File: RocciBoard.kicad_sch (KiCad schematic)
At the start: 205 parts, among them J1 Battery, J10 M3, J11 I2C6, J12 Power, J13 M2, J14 I2C7, J2 I2C0, J3 I2C1, J4 I2C2, J5 I2C3, J6 M0, J7 I2C4, J8 M1, J9 I2C5, Q1 IRF 7424, Q2 2N7002, SW1 SW_DIP_x01, U1 LMR33630, U10 LM317_TO-252, U11 CJ431, U12 CJ431, U2 LM317_TO-252, U3 LM317_TO-252, U4 TPS3700, U5 TCA9548A, U6 DRV8871, U7 DRV8871, U8 DRV8871, U9 DRV8871

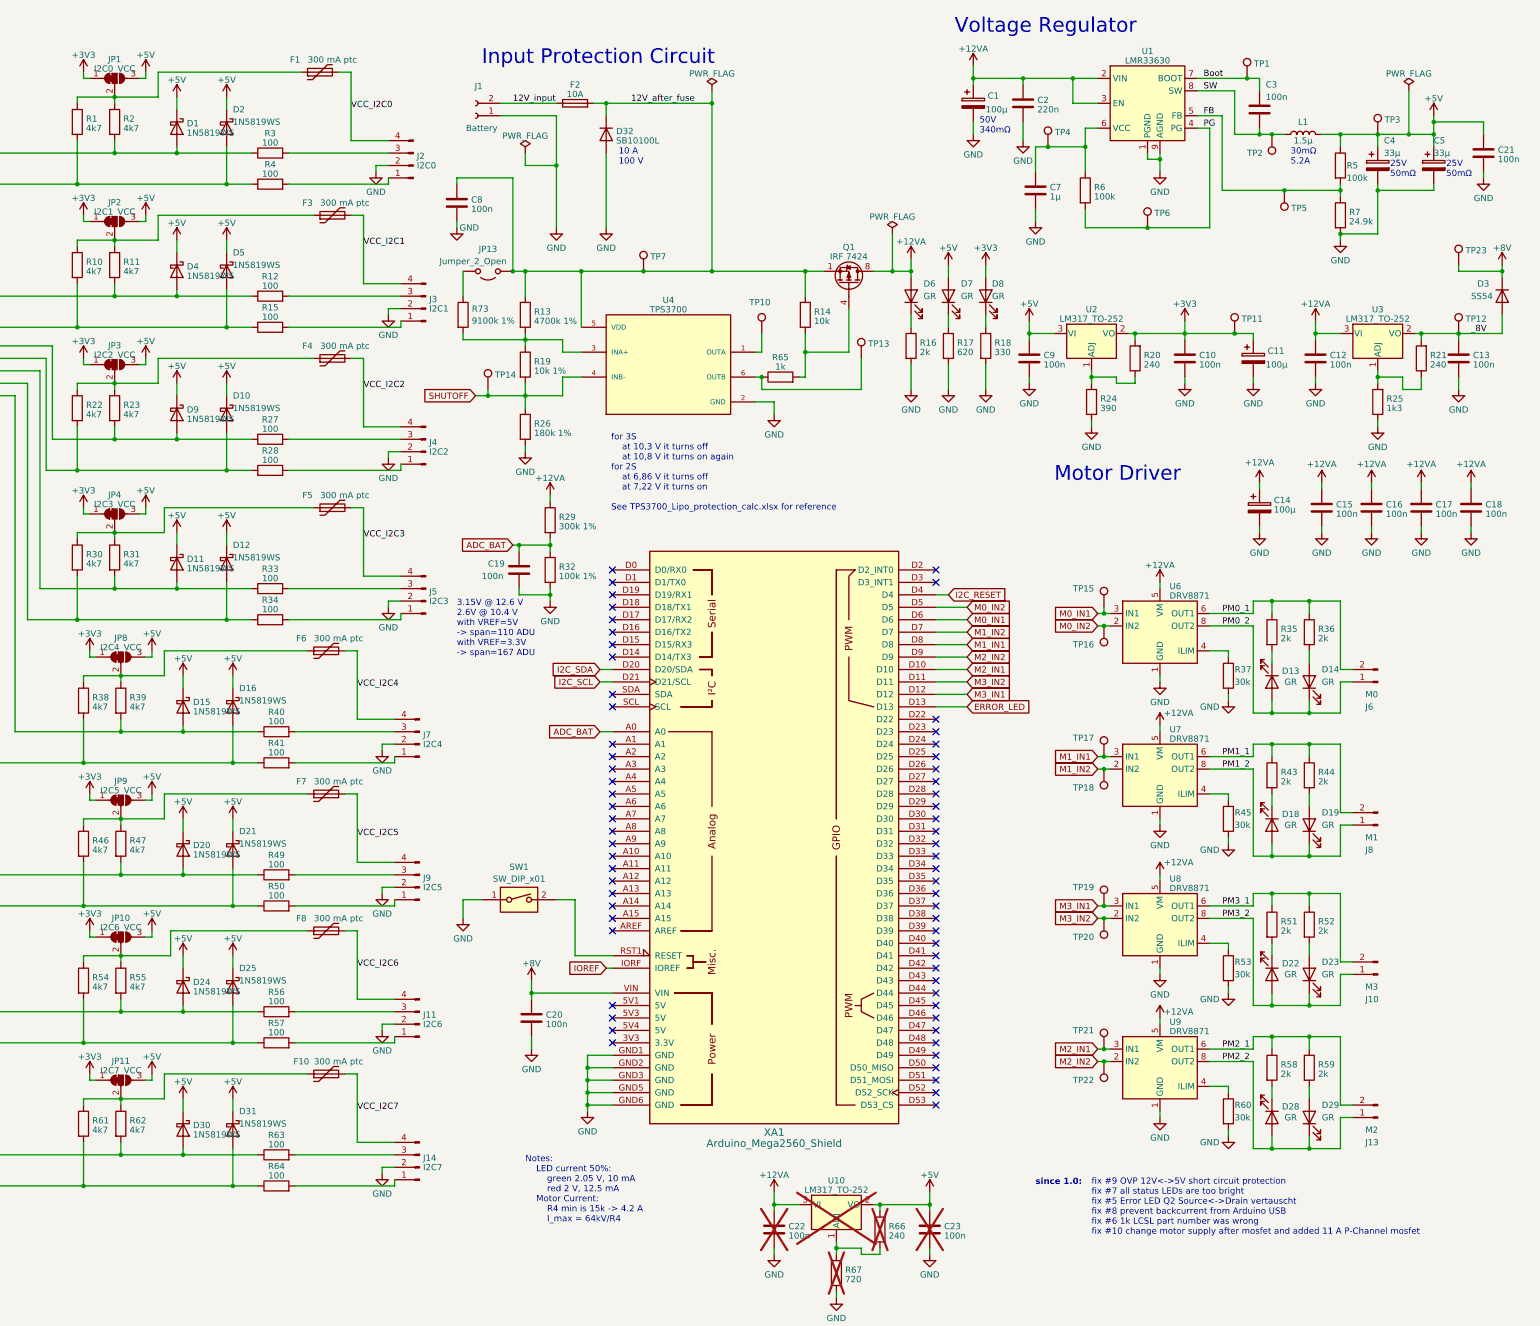
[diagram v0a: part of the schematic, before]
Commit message: add xt60 and spereate i2c pwr and data jumper
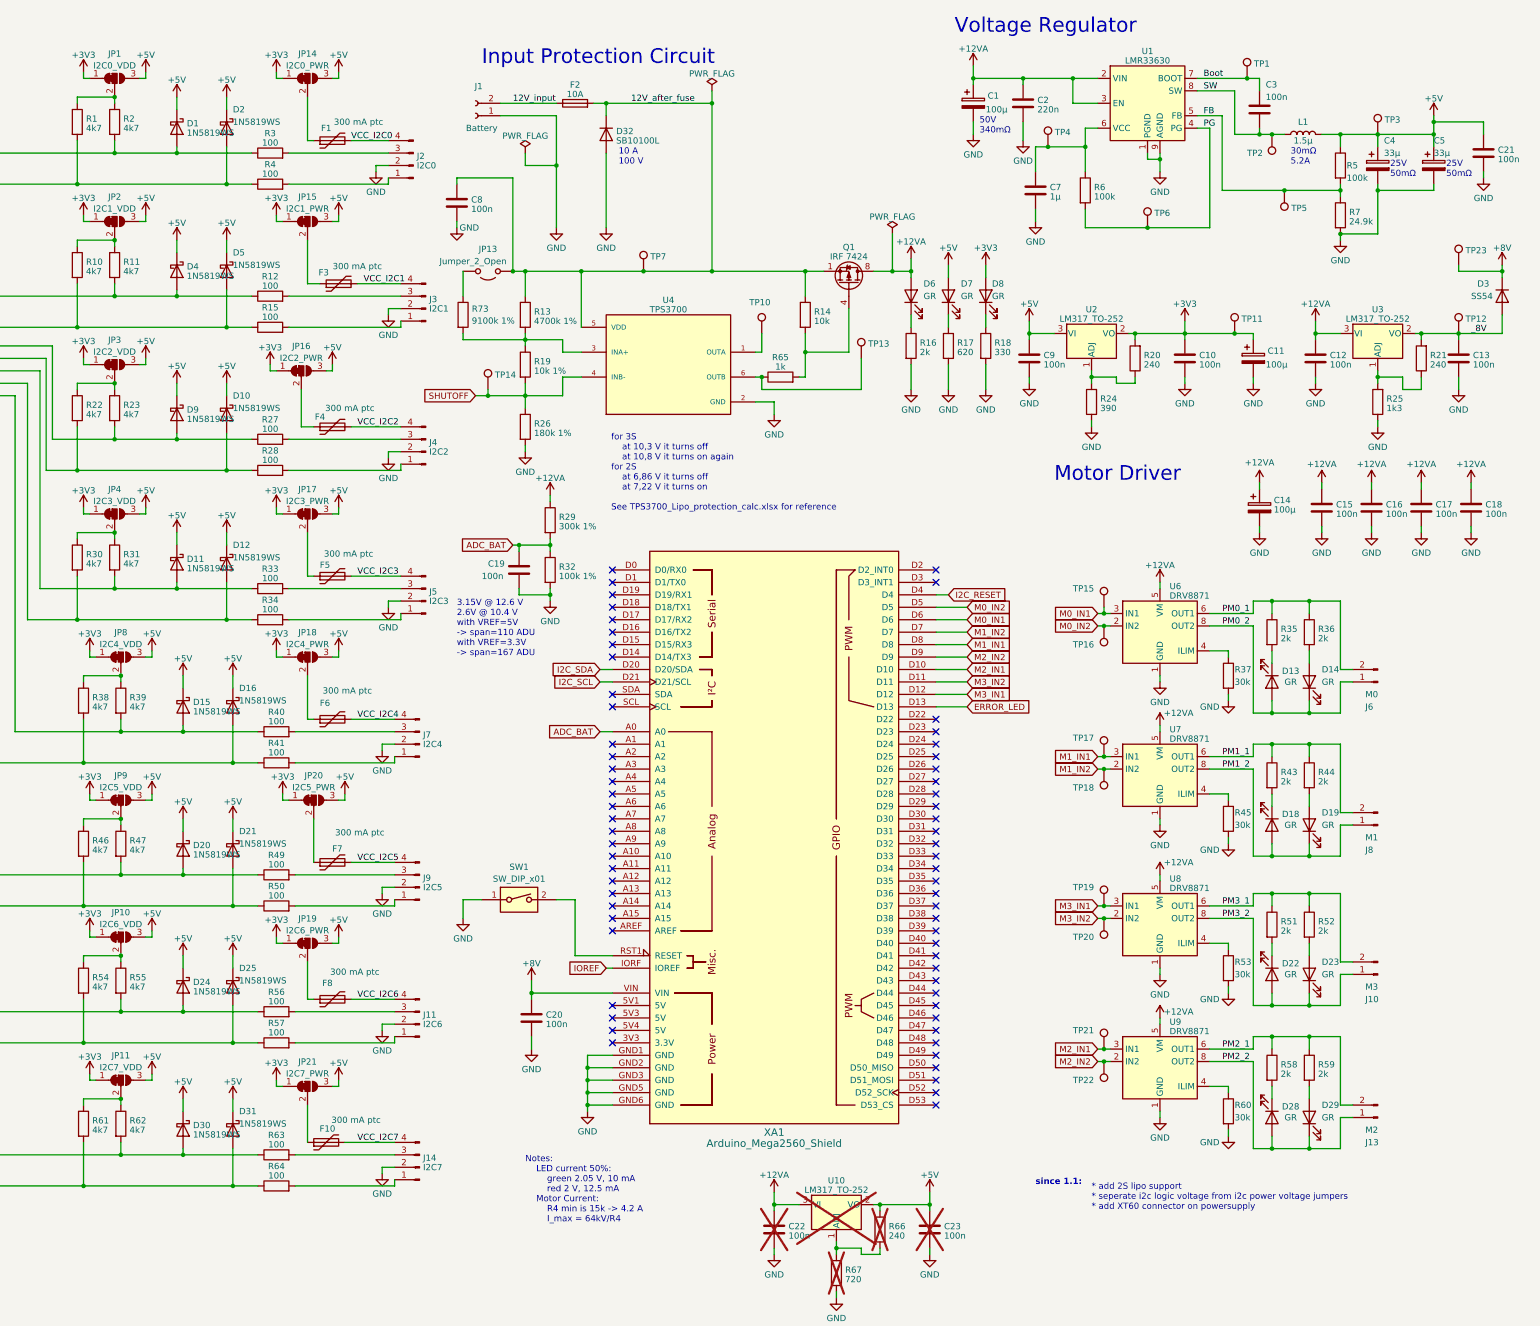
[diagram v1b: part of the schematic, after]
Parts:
- added JP14: I2C0_PWR, Jumper:SolderJumper-3_P1.3mm_Open_Pad1.0x1.5mm, symbol Jumper:SolderJumper_3_Bridged12
- added JP15: I2C1_PWR, Jumper:SolderJumper-3_P1.3mm_Open_Pad1.0x1.5mm, symbol Jumper:SolderJumper_3_Bridged12
- added JP16: I2C2_PWR, Jumper:SolderJumper-3_P1.3mm_Open_Pad1.0x1.5mm, symbol Jumper:SolderJumper_3_Bridged12
- added JP17: I2C3_PWR, Jumper:SolderJumper-3_P1.3mm_Open_Pad1.0x1.5mm, symbol Jumper:SolderJumper_3_Bridged12
- added JP18: I2C4_PWR, Jumper:SolderJumper-3_P1.3mm_Open_Pad1.0x1.5mm, symbol Jumper:SolderJumper_3_Bridged12
- added JP19: I2C6_PWR, Jumper:SolderJumper-3_P1.3mm_Open_Pad1.0x1.5mm, symbol Jumper:SolderJumper_3_Bridged12
- added JP20: I2C5_PWR, Jumper:SolderJumper-3_P1.3mm_Open_Pad1.0x1.5mm, symbol Jumper:SolderJumper_3_Bridged12
- added JP21: I2C7_PWR, Jumper:SolderJumper-3_P1.3mm_Open_Pad1.0x1.5mm, symbol Jumper:SolderJumper_3_Bridged12
- J1: footprint Connector_Phoenix_MSTB:PhoenixContact_MSTBVA_2,5_2-G_1x02_P5.00mm_Vertical -> Connector_AMASS:AMASS_XT60-M_1x02_P7.20mm_Vertical
- JP1: value I2C0_VCC -> I2C0_VDD
- JP10: value I2C6_VCC -> I2C6_VDD
- JP11: value I2C7_VCC -> I2C7_VDD
- JP13: footprint (none) -> Jumper:SolderJumper-2_P1.3mm_Open_Pad1.0x1.5mm
- JP2: value I2C1_VCC -> I2C1_VDD
- JP3: value I2C2_VCC -> I2C2_VDD
- JP4: value I2C3_VCC -> I2C3_VDD
- JP8: value I2C4_VCC -> I2C4_VDD
- JP9: value I2C5_VCC -> I2C5_VDD
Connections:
- net +3V3: now also JP14.1 (A), JP15.1 (A), JP16.1 (A), JP17.1 (A), JP18.1 (A), JP19.1 (A), JP20.1 (A), JP21.1 (A)
- net +5V: now also JP14.3 (B), JP15.3 (B), JP16.3 (B), JP17.3 (B), JP18.3 (B), JP19.3 (B), JP20.3 (B), JP21.3 (B)
- net at JP11.2 (C), R61.1, R62.1: no longer F10.1
- net at JP3.2 (C), R22.1, R23.1: no longer F4.1
- net at JP10.2 (C), R54.1, R55.1: no longer F8.1
- net at JP2.2 (C), R10.1, R11.1: no longer F3.1
- net at JP8.2 (C), R38.1, R39.1: no longer F6.1
- net at JP1.2 (C), R1.1, R2.1: no longer F1.1
- net at JP9.2 (C), R46.1, R47.1: no longer F7.1
- net at JP4.2 (C), R30.1, R31.1: no longer F5.1
- new net: F5.1, JP17.2 (C)
- new net: F1.1, JP14.2 (C)
- new net: F6.1, JP18.2 (C)
- new net: F10.1, JP21.2 (C)
- new net: F8.1, JP19.2 (C)
- new net: F4.1, JP16.2 (C)
- new net: F3.1, JP15.2 (C)
- new net: F7.1, JP20.2 (C)
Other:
- note added: "* add 2S lipo support * seperate i2c logic voltage from i2c power voltage jumpers * add XT60 connector on powersupply"
- note added: "since 1.1:"
- note removed: "fix #9 OVP 12V<->5V short circuit protection fix #7 all status LEDs are too bright fix #5 Error LED Q2 Source<->Drain vertauscht fix #8 prevent backcurrent from Arduino USB fix #6 1k LCSL part number was wrong fix #10 change motor supply after mosfet and added 11 A P-Channel mosfet"
- note removed: "since 1.0:"
- moved on the sheet: F1, F10, F3, F4, F5, F6, F7, F8

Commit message: more progress with nxt shield
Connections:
- net VCC_UF_I2C3: now reaches F5.1, JP17.2 (C)
- net VCC_UF_I2C0: now reaches F1.1, JP14.2 (C)
- net VCC_UF_I2C4: now reaches F6.1, JP18.2 (C)
- net VCC_UF_I2C7: now reaches F10.1, JP21.2 (C)
- net VCC_UF_I2C6: now reaches F8.1, JP19.2 (C)
- net VCC_UF_I2C2: now reaches F4.1, JP16.2 (C)
- net VCC_UF_I2C1: now reaches F3.1, JP15.2 (C)
- net VCC_UF_I2C5: now reaches F7.1, JP20.2 (C)
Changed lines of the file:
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@@
+		)
+	)
+	(label "VCC_UF_I2C1"
+		(at 158.75 65.0989 0)
+		(effects
+			(font
+				(size 1.27 1.27)
+			)
+			(justify left bottom)
 		)
 	)
@@
 		)
 	)
+	(label "VCC_UF_I2C4"
+		(at 158.75 152.4 0)
+		(effects
+			(font
+				(size 1.27 1.27)
+			)
+			(justify left bottom)
+		)
+	)
+	(label "VCC_UF_I2C0"
+		(at 158.75 35.56 0)
+		(effects
+			(font
+				(size 1.27 1.27)
+			)
+			(justify left bottom)
+		)
+	)
 	(label "VCC_I2C4"
 		(at 168.91 160.02 0)
@@
 		)
 	)
+	(label "VCC_UF_I2C6"
+		(at 158.75 209.55 0)
+		(effects
+			(font
+				(size 1.27 1.27)
+			)
+			(justify left bottom)
+		)
+	)
 	(label "PM3_2"
 		(at 345.44 200.66 0)
@@
 		)
 	)
+	(label "VCC_UF_I2C3"
+		(at 158.75 123.19 0)
+		(effects
+			(font
+				(size 1.27 1.27)
+			)
+			(justify left bottom)
+		)
+	)
 	(label "VCC_I2C1"
 		(at 170.18 71.12 0)
@@
 		)
 	)
+	(label "VCC_UF_I2C5"
+		(at 160.02 181.61 0)
+		(effects
+			(font
+				(size 1.27 1.27)
+			)
+			(justify left bottom)
+		)
+	)
 	(label "VCC_I2C5"
 		(at 168.91 189.23 0)
@@
 		)
 	)
+	(label "VCC_UF_I2C2"
+		(at 157.48 95.25 0)
+		(effects
+			(font
+				(size 1.27 1.27)
+			)
+			(justify left bottom)
+		)
+	)
 	(label "VCC_I2C7"
 		(at 168.91 246.38 0)
 		(effects
 			(font
+				(size 1.27 1.27)
+			)
+			(justify left bottom)
+		)
+	)
+	(label "VCC_UF_I2C7"
+		(at 158.75 240.03 0)
+		(effects
+			(font

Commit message: Version 1.2 finished
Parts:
- removed C22, C23: 100n, Capacitor_SMD:C_0603_1608Metric, symbol Device:C
- removed D32: SB10100L, Package_TO_SOT_SMD:TO-277A, symbol Diode:VS-6ESU06
- removed D33: BT137S-600E, Package_TO_SOT_SMD:TO-252-2, symbol Device:Q_TRIAC_A1A2G
- removed F2: 10A, Fuse:Fuseholder_Cylinder-5x20mm_Wuerth_696103101002-SMD_Horizontal_Open, symbol Device:Fuse
- removed Q1: IRF 7424, Package_SO:SOIC-8_3.9x4.9mm_P1.27mm, symbol Transistor_FET:IRF7404
- removed R20: 240, Resistor_SMD:R_0603_1608Metric, symbol Device:R
- removed R24: 390, Resistor_SMD:R_0603_1608Metric, symbol Device:R
- removed R69: 1k5, Resistor_SMD:R_0603_1608Metric, symbol Device:R
- removed R70: 1k3, Resistor_SMD:R_0603_1608Metric, symbol Device:R
- removed R71: 1k, Resistor_SMD:R_0603_1608Metric, symbol Device:R
- removed R72: 2k, Resistor_SMD:R_0603_1608Metric, symbol Device:R
- removed U10, U2, U3: LM317_TO-252, Package_TO_SOT_SMD:TO-252-2, symbol Regulator_Linear:LM317_TO-252
- removed U11, U12: CJ431, Package_TO_SOT_SMD:SOT-23, symbol Reference_Voltage:TL432DBZ
- removed U4: TPS3700, Package_TO_SOT_SMD:SOT-23-6, symbol TPS3700DDCR:TPS3700DDCR
- added C24, C25, C27: 10nF, Capacitor_SMD:C_0603_1608Metric, symbol Device:C
- added C26, C29, C30: 100nF, Capacitor_SMD:C_0603_1608Metric, symbol Device:C
- added C28: 47pF, Capacitor_SMD:C_0603_1608Metric, symbol Device:C
- added D26: 1N5819WS, Diode_SMD:D_SOD-323, symbol Diode:BAT42
- added JP22: Jumper_2_Open, Jumper:SolderJumper-2_P1.3mm_Open_Pad1.0x1.5mm, symbol Jumper:Jumper_2_Open
- added Q1, Q3: TM30N03D, Package_TO_SOT_SMD:TO-252-2, symbol Transistor_FET:Q_NMOS_GDS
- added R74: 4.7k, Resistor_SMD:R_0603_1608Metric, symbol Device:R
- added R75: 51, Resistor_SMD:R_0603_1608Metric, symbol Device:R
- added R76: 0, Resistor_SMD:R_0603_1608Metric, symbol Device:R
- added R77: 100, Resistor_SMD:R_0603_1608Metric, symbol Device:R
- added R78, R83: 68k, Resistor_SMD:R_0603_1608Metric, symbol Device:R
- added R79: 24k, Resistor_SMD:R_0603_1608Metric, symbol Device:R
- added R80: 2.7k, Resistor_SMD:R_0603_1608Metric, symbol Device:R
- added R81: 510k, Resistor_SMD:R_0603_1608Metric, symbol Device:R
- added R82: 12k, Resistor_SMD:R_0603_1608Metric, symbol Device:R
- added U10, U13: TPS3700, Package_TO_SOT_SMD:SOT-23-6, symbol custom_parts:TPS3700
- added U11: AMS1117-3.3, Package_TO_SOT_SMD:SOT-223-3_TabPin2, symbol Regulator_Linear:AMS1117-3.3
- added U14: AMS1117, Package_TO_SOT_SMD:SOT-223-3_TabPin2, symbol Regulator_Linear:AMS1117
- added U4: LM74900, Package_DFN_QFN:VQFN-24-1EP_4x4mm_P0.5mm_EP2.5x2.5mm_ThermalVias, symbol custom_parts:LM74900
- D13, D14, D18, D19, D22, D23, D28, D29, D6, D7, D8: LCSC C72043 -> C965805
- Q2: symbol Device:Q_NMOS_GSD -> Transistor_FET:Q_NMOS_GSD
- R13: value 4700k 1% -> 100k; LCSC C23163 -> C25803
- R14: value 10k -> 1mΩ 1%; footprint Resistor_SMD:R_0603_1608Metric -> Resistor_SMD:R_1206_3216Metric; LCSC C25804 -> C7467246
- R17: value 620 -> 680
- R19: value 10k 1% -> 100k; LCSC C25804 -> C25803
- R21: value 240 -> 200; LCSC C23350 -> C8218
- R25: value 1k3 -> 1k; LCSC C22767 -> C21190
- R26: value 180k 1% -> 3.9k; LCSC C22827 -> C23018
- R65: value 1k -> 100k; LCSC C21190 -> C25803
- R66: value 240 -> 7,5k; LCSC C23350 -> C23234; now fitted; now in the parts list
- R67: value 720 -> 39k; LCSC C23151 -> C23153; now fitted; now in the parts list
- R68: value 1k -> 470k; LCSC C21190 -> C23178; now fitted
- R7: value 24.9k -> 33k; LCSC C25962 -> C4216
- R73: value 9100k 1% -> 3.3k; LCSC C23163 -> C22978
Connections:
- net +12VA: now also Q1.3 (S), U14.3 (VI), U4.15 (OUT), U4.16 (SLEEP_OV); no longer R68.1
- net +3V3: now also U11.2 (VO)
- net +5V: now also U11.3 (VI); no longer R66.2
- net 12V_input: now also C8.1, D26.2 (A), Q3.3 (S), U4.2 (A)
- net GND: now also JP13.2 (B), R65.1, R67.2, R73.2, C27.2, C28.2, C29.1, C30.2, JP22.2 (B), R78.1, R79.1, R80.2, R83.2, U10.2 (GND), U11.1 (GND), U13.2 (GND), U4.13 (GND); no longer R26.2, R67.1
- net SHUTOFF: now also R13.2, R74.1, U4.4 (UVLO); no longer R19.2, R26.1, TP14.1
- net _8V: now also U14.2 (VO)
- net at R66.1: now also R68.2, U10.4 (INBM); no longer R67.2
- net at R65.2: now also C28.1, U4.9 (TMR); no longer R14.2
- net 5V_unfused: now reaches F9.2, J12.2 (Pin_2)
- net 5V_unfused: now also R68.1
- net 3V3_unfused: now reaches F11.2, J12.3 (Pin_3)
- net 3V3_unfused: now also R81.1
- net at TP13.1: now also R79.2, U4.10 (IMON); no longer R65.1
- net at R21.1, R25.2: now also U14.1 (ADJ)
- net at TP10.1: now also U4.7 (INV_SLEEP)
- net at JP12.2 (B): now also U10.1 (OUTA), U10.6 (OUTB), U13.1 (OUTA), U13.6 (OUTB); no longer R68.2
- net at R73.1: now also JP13.1 (A), R74.2; no longer JP13.2 (B)
- removed net 12V_after_fuse: C8.1, JP13.1 (A), R13.1, R14.1, TP7.1
- new net: D26.1 (K), U10.5 (VDD), U13.5 (VDD)
- new net: R66.2, R67.1, U10.3 (INAP)
- new net: C27.1, R77.1
- new net: JP22.1 (A), R26.2, R80.1
- new net: C26.1, C29.2, Q3.2 (D), R14.1, R75.2, R76.2, U4.22 (VS), U4.24 (C)
- new net: C26.2, U4.23 (CAP)
- new net: R78.2, U4.11 (ILM)
- new net: R81.2, R82.1, U13.4 (INBM)
- new net: C24.1, R75.1, U4.20 (CS+)
- new net: TP7.1, U4.12 (INV_FLT)
- new net: Q3.1 (G), U4.1 (DGATE)
- new net: Q1.1 (G), R77.2, U4.14 (HGATE)
- new net: C25.1, R76.1, U4.18 (ISCP)
- new net: C24.2, C25.2, Q1.2 (D), R14.2, U4.19 (CS-)
- new net: R13.1, R19.1, U4.3 (SW)
- new net: C30.1, R19.2, R26.1, U4.5 (OV)
- new net: TP14.1, U4.6 (EN)
- new net: R82.2, R83.1, U13.3 (INAP)
- no-connect marks 64 -> 67
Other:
- note added: "* add 2S lipo support * seperate i2c logic voltage from i2c power voltage jumpers * add XT60 connector on powersupply * change fuse to Efuse and added voltage monitor for supply"
- note added: "60k -> 10A OCP"
- note added: "Mosfet Specs: ~ 15nC@10V > 20A I_DS > 30V VDS < 10V VGS_th"
- note added: "UVLO_3S = 11,13 UVLO_2S = 6,75 OVP_3S = 15.9V OVP_2S = 9.6V See LM75900_Lipo_protection_calc.xlsx for reference"
- note removed: "* add 2S lipo support * seperate i2c logic voltage from i2c power voltage jumpers * add XT60 connector on powersupply"
- note removed: "10 A 100 V"
- note removed: "for 3S at 10,3 V it turns off at 10,8 V it turns on again for 2S at 6,86 V it turns off at 7,22 V it turns on See TPS3700_Lipo_protection_calc.xlsx for reference"
- moved on the sheet: C1, C10, C11, C12, C13, C14, C15, C16, C17, C18, C19, C2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
